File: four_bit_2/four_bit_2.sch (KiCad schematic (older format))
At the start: 1 part, among them P1 DIN_41612_128P

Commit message: Added in WHOMP, whatever it is
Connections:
- net CI09/: now also P1.60 (28B); no longer P1.59 (27B)
- net CO10: now also P1.61 (29B); no longer P1.60 (28B)
- net G05/: now also P1.62 (30B); no longer P1.61 (29B)
- net G06/: now also P1.63 (31B); no longer P1.62 (30B)
- net G07/: now also P1.64 (32B); no longer P1.63 (31B)
- net GND: no longer P1.71 (7C)
- net L08/: now also P1.65 (1C); no longer P1.64 (32B)
- net WL05/: now also P1.68 (4C); no longer P1.67 (3C)
- net WL06/: now also P1.69 (5C); no longer P1.68 (4C)
- net WL07/: now also P1.70 (6C); no longer P1.69 (5C)
- net WL08/: now also P1.71 (7C); no longer P1.70 (6C)
- net XUY05/: now also P1.66 (2C); no longer P1.65 (1C)
- net XUY06/: now also P1.67 (3C); no longer P1.66 (2C)
- new net WHOMP: P1.59 (27B)
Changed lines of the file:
@@
 $EndDescr
 $Sheet
-S 1750 1200 1400 7250
+S 1750 1200 1400 7600
 U 5692835C
 F0 "A09_1" 60
@@
 F60 "_WL1" O R 3150 4050 60
 F61 "_WL1/" O R 3150 4150 60
-F62 "_MWL1" O R 3150 4600 60
+F62 "_MWL1" O R 3150 4750 60
 F63 "_CI_OUT" O R 3150 2750 60
 F64 "_CO_IN" I L 1750 3650 60
@@
 F96 "_WL2" O R 3150 4250 60
 F97 "_WL2/" O R 3150 4350 60
-F98 "_MWL2" O R 3150 4700 60
+F98 "_MWL2" O R 3150 4850 60
 F99 "_RL1/" O R 3150 3850 60
 F100 "_RL2/" O R 3150 3950 60
+F101 "_RL_OUT_2" O R 3150 4600 60
+F102 "_RL_OUT_1" O R 3150 4500 60
+F103 "_WHOMPA" I L 1750 8700 60
+F104 "_WHOMP_1" I L 1750 8500 60
+F105 "_WHOMP_2" I L 1750 8600 60
 $EndSheet
 $Comp
@@
 $EndComp
 $Sheet
-S 4400 1200 1400 7250
+S 4400 1200 1400 7600
 U 56928367
 F0 "A09_2" 60
@@
 F60 "_WL1" O R 5800 4050 60
 F61 "_WL1/" O R 5800 4150 60
-F62 "_MWL1" O R 5800 4600 60
+F62 "_MWL1" O R 5800 4700 60
 F63 "_CI_OUT" O R 5800 2750 60
 F64 "_CO_IN" I L 4400 3650 60
@@
 F96 "_WL2" O R 5800 4250 60
 F97 "_WL2/" O R 5800 4350 60
-F98 "_MWL2" O R 5800 4700 60
+F98 "_MWL2" O R 5800 4850 60
 F99 "_RL1/" O R 5800 3850 60
 F100 "_RL2/" O R 5800 3950 60
+F101 "_RL_OUT_2" O R 5800 4600 60
+F102 "_RL_OUT_1" O R 5800 4500 60
+F103 "_WHOMPA" I L 4400 8700 60
+F104 "_WHOMP_1" I L 4400 8500 60
+F105 "_WHOMP_2" I L 4400 8600 60
 $EndSheet
 Text GLabel 1650 1300 0    60   Input ~ 0
@@
 	4400 8350 4300 8350
 Wire Wire Line
-	9700 1550 9800 1550
-Wire Wire Line
 	9700 1650 9800 1650
-Connection ~ 9700 1650
 Wire Wire Line
 	9700 1750 9800 1750
@@
 Wire Wire Line
 	5800 1800 5900 1800
-Text GLabel 8750 3750 0    60   Input ~ 0
+Text GLabel 8750 3850 0    60   Input ~ 0
 G05/
-Text GLabel 8750 3850 0    60   Input ~ 0
+Text GLabel 8750 3950 0    60   Input ~ 0
 G06/
-Text GLabel 8750 3950 0    60   Input ~ 0
+Text GLabel 8750 4050 0    60   Input ~ 0
 G07/
 Wire Wire Line
-	8850 3750 8750 3750
-Wire Wire Line
 	8850 3850 8750 3850
 Wire Wire Line
 	8850 3950 8750 3950
 Wire Wire Line
-	9700 1550 9700 4200
+	8850 4050 8750 4050
+Wire Wire Line
+	9700 1650 9700 4200
 Text GLabel 3250 3350 2    60   Output ~ 0
 XUY05/
@@
 Wire Wire Line
 	3150 3450 3250 3450
-Text GLabel 9700 950  0    60   Input ~ 0
+Text GLabel 9700 1050 0    60   Input ~ 0
 XUY05/
-Text GLabel 9700 1050 0    60   Input ~ 0
+Text GLabel 9700 1150 0    60   Input ~ 0
 XUY06/
 Wire Wire Line
-	8850 4050 8750 4050
-Wire Wire Line
-	9800 1050 9700 1050
-Text GLabel 9700 1150 0    60   Input ~ 0
-WL05/
+	9800 950  9700 950
 Wire Wire Line
 	9800 1150 9700 1150
 Text GLabel 9700 1250 0    60   Input ~ 0
-WL06/
+WL05/
 Wire Wire Line
 	9800 1250 9700 1250
 Text GLabel 9700 1350 0    60   Input ~ 0
-WL07/
+WL06/
 Wire Wire Line
 	9800 1350 9700 1350
 Text GLabel 9700 1450 0    60   Input ~ 0
+WL07/
+Wire Wire Line
+	9800 1450 9700 1450
+Text GLabel 9700 1550 0    60   Input ~ 0
 WL08/
 Wire Wire Line
-	9800 1450 9700 1450
+	9800 1550 9700 1550
 Text GLabel 5900 2750 2    60   Output ~ 0
 CI09/
@@
 Wire Wire Line
 	5800 2850 5900 2850
-Text GLabel 8750 3550 0    60   Input ~ 0
+Text GLabel 8750 3650 0    60   Input ~ 0
 CI09/
-Text GLabel 8750 3650 0    60   Input ~ 0
+Text GLabel 8750 3750 0    60   Input ~ 0
 CO10
 Wire Wire Line
-	8850 3550 8750 3550
-Wire Wire Line
 	8850 3650 8750 3650
+Wire Wire Line
+	8850 3750 8750 3750
 Text Label 3250 2200 0    60   ~ 0
 L06/
@@
 	5800 2200 5900 2200
 Wire Wire Line
-	9700 950  9800 950
-Text GLabel 8750 4050 0    60   Input ~ 0
+	9700 1050 9800 1050
+Text GLabel 9700 950  0    60   Input ~ 0
 L08/
+Wire Wire Line
+	1750 8600 1200 8600
+Wire Wire Line
+	1200 8500 1200 8750
+Wire Wire Line
+	1750 8700 1200 8700
+Connection ~ 1200 8700
+$Comp
+L GND #PWR011
+U 1 1 56C64D2D
+P 1200 8750
+F 0 "#PWR011" H 1200 8500 50  0001 C CNN
+F 1 "GND" H 1200 8600 50  0000 C CNN
+F 2 "" H 1200 8750 60  0000 C CNN
+F 3 "" H 1200 8750 60  0000 C CNN
+	1    1200 8750
+	1    0    0    -1
+$EndComp
+Wire Wire Line
+	1200 8500 1750 8500
+Connection ~ 1200 8600
+Wire Wire Line
+	4400 8600 3850 8600
+Wire Wire Line
+	3850 8600 3850 8750
+Wire Wire Line
+	4400 8700 3850 8700
+Connection ~ 3850 8700
+$Comp
+L GND #PWR012
+U 1 1 56C696A6
+P 3850 8750
+F 0 "#PWR012" H 3850 8500 50  0001 C CNN
+F 1 "GND" H 3850 8600 50  0000 C CNN
+F 2 "" H 3850 8750 60  0000 C CNN
+F 3 "" H 3850 8750 60  0000 C CNN
+	1    3850 8750
+	1    0    0    -1
+$EndComp
+Text GLabel 4300 8500 0    60   Input ~ 0
+WHOMP
+Wire Wire Line
+	4400 8500 4300 8500
+Text GLabel 8750 3550 0    60   Output ~ 0
+WHOMP
+Wire Wire Line
+	8850 3550 8750 3550
 $EndSCHEMATC

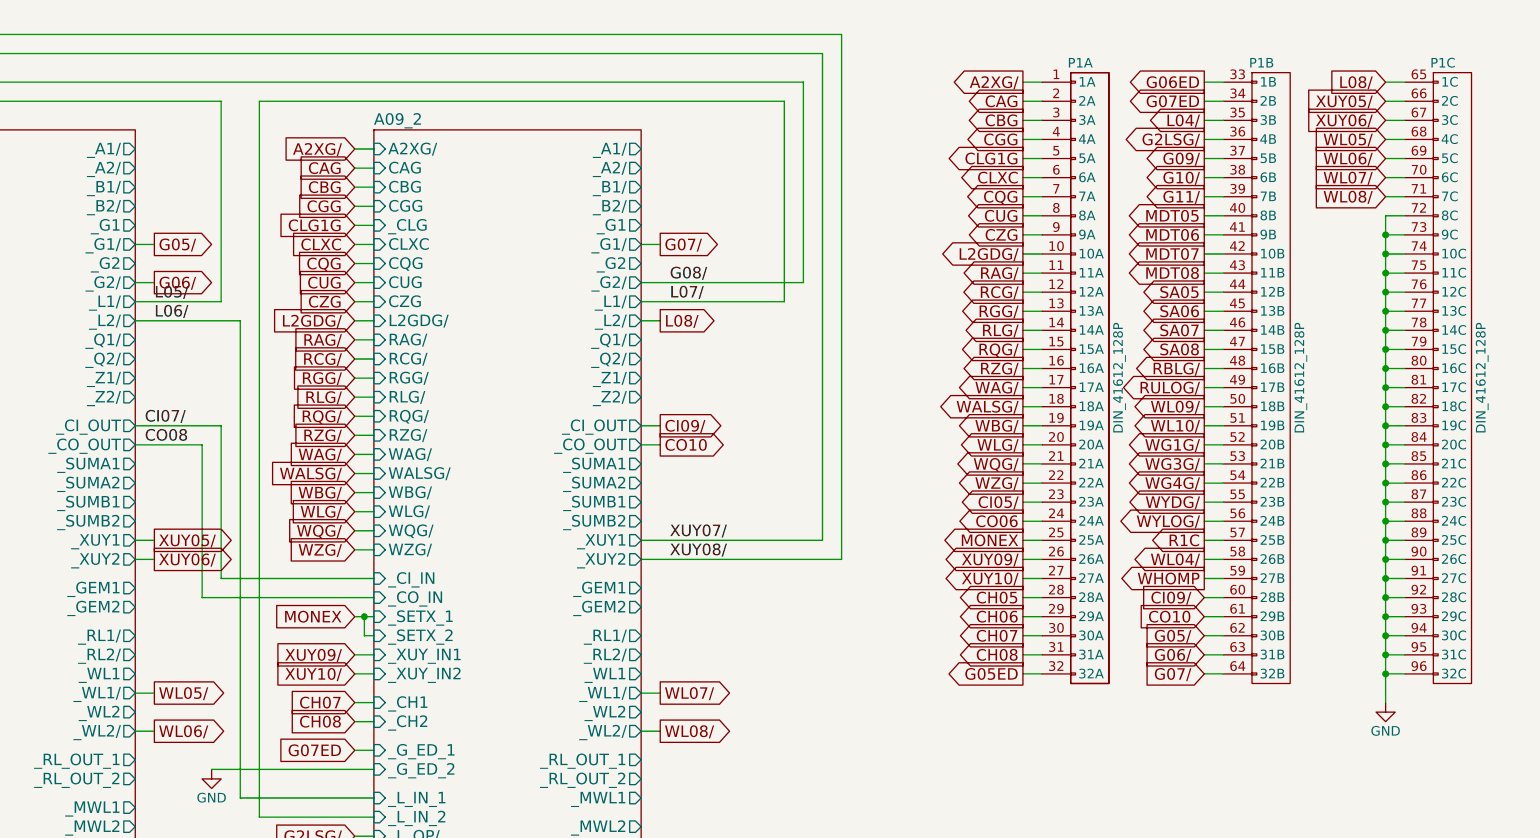
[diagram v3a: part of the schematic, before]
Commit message: Added and tied in module 12, parity & s register
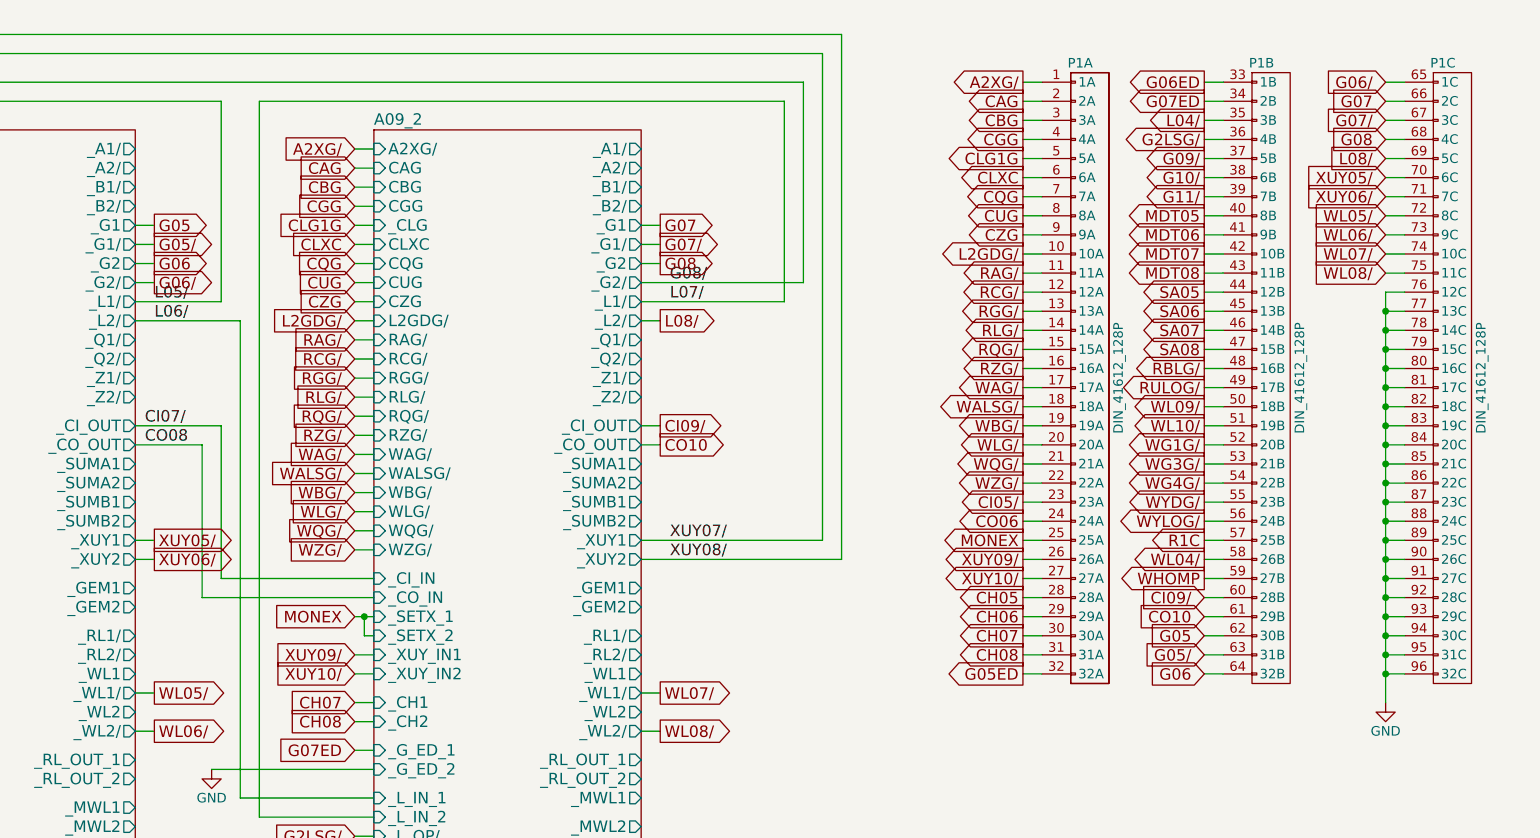
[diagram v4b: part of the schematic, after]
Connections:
- net G05/: now also P1.63 (31B); no longer P1.62 (30B)
- net G06/: now also P1.65 (1C); no longer P1.63 (31B)
- net G07/: now also P1.67 (3C); no longer P1.64 (32B)
- net GND: no longer P1.72 (8C), P1.73 (9C), P1.74 (10C), P1.75 (11C)
- net L08/: now also P1.69 (5C); no longer P1.65 (1C)
- net WL05/: now also P1.72 (8C); no longer P1.68 (4C)
- net WL06/: now also P1.73 (9C); no longer P1.69 (5C)
- net WL07/: now also P1.74 (10C); no longer P1.70 (6C)
- net WL08/: now also P1.75 (11C); no longer P1.71 (7C)
- net XUY05/: now also P1.70 (6C); no longer P1.66 (2C)
- net XUY06/: now also P1.71 (7C); no longer P1.67 (3C)
- new net G05: P1.62 (30B)
- new net G06: P1.64 (32B)
- new net G07: P1.66 (2C)
- new net G08: P1.68 (4C)
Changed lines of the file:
@@
 	4400 8350 4300 8350
 Wire Wire Line
-	9700 1650 9800 1650
-Wire Wire Line
-	9700 1750 9800 1750
-Connection ~ 9700 1750
-Wire Wire Line
-	9700 1850 9800 1850
-Connection ~ 9700 1850
-Wire Wire Line
-	9700 1950 9800 1950
-Connection ~ 9700 1950
-Wire Wire Line
 	9700 2050 9800 2050
-Connection ~ 9700 2050
 Wire Wire Line
 	9700 2150 9800 2150
@@
 Wire Wire Line
 	5800 1800 5900 1800
-Text GLabel 8750 3850 0    60   Input ~ 0
+Text GLabel 8750 3950 0    60   Input ~ 0
 G05/
-Text GLabel 8750 3950 0    60   Input ~ 0
+Text GLabel 9700 950  0    60   Input ~ 0
 G06/
-Text GLabel 8750 4050 0    60   Input ~ 0
+Text GLabel 9700 1150 0    60   Input ~ 0
 G07/
 Wire Wire Line
-	8850 3850 8750 3850
-Wire Wire Line
 	8850 3950 8750 3950
 Wire Wire Line
-	8850 4050 8750 4050
-Wire Wire Line
-	9700 1650 9700 4200
+	9800 950  9700 950
+Wire Wire Line
+	9800 1150 9700 1150
 Text GLabel 3250 3350 2    60   Output ~ 0
 XUY05/
@@
 Wire Wire Line
 	3150 3450 3250 3450
-Text GLabel 9700 1050 0    60   Input ~ 0
+Text GLabel 9700 1450 0    60   Input ~ 0
 XUY05/
-Text GLabel 9700 1150 0    60   Input ~ 0
+Text GLabel 9700 1550 0    60   Input ~ 0
 XUY06/
 Wire Wire Line
-	9800 950  9700 950
-Wire Wire Line
-	9800 1150 9700 1150
-Text GLabel 9700 1250 0    60   Input ~ 0
+	9800 1350 9700 1350
+Wire Wire Line
+	9800 1550 9700 1550
+Text GLabel 9700 1650 0    60   Input ~ 0
 WL05/
 Wire Wire Line
-	9800 1250 9700 1250
-Text GLabel 9700 1350 0    60   Input ~ 0
+	9800 1650 9700 1650
+Text GLabel 9700 1750 0    60   Input ~ 0
 WL06/
 Wire Wire Line
-	9800 1350 9700 1350
-Text GLabel 9700 1450 0    60   Input ~ 0
+	9800 1750 9700 1750
+Text GLabel 9700 1850 0    60   Input ~ 0
 WL07/
 Wire Wire Line
-	9800 1450 9700 1450
-Text GLabel 9700 1550 0    60   Input ~ 0
+	9800 1850 9700 1850
+Text GLabel 9700 1950 0    60   Input ~ 0
 WL08/
 Wire Wire Line
-	9800 1550 9700 1550
+	9800 1950 9700 1950
 Text GLabel 5900 2750 2    60   Output ~ 0
 CI09/
@@
 	5800 2200 5900 2200
 Wire Wire Line
-	9700 1050 9800 1050
-Text GLabel 9700 950  0    60   Input ~ 0
+	9700 1450 9800 1450
+Text GLabel 9700 1350 0    60   Input ~ 0
 L08/
 Wire Wire Line
@@
 Wire Wire Line
 	8850 3550 8750 3550
+Text GLabel 3250 1700 2    60   Output ~ 0
+G05
+Wire Wire Line
+	3150 1700 3250 1700
+Text GLabel 3250 1900 2    60   Output ~ 0
+G06
+Wire Wire Line
+	3150 1900 3250 1900
+Text GLabel 5900 1700 2    60   Output ~ 0
+G07
+Wire Wire Line
+	5800 1700 5900 1700
+Text GLabel 5900 1900 2    60   Output ~ 0
+G08
+Wire Wire Line
+	5800 1900 5900 1900
+Wire Wire Line
+	9700 2050 9700 4200
+Text GLabel 8750 3850 0    60   Input ~ 0
+G05
+Wire Wire Line
+	8850 3850 8750 3850
+Text GLabel 8750 4050 0    60   Input ~ 0
+G06
+Wire Wire Line
+	8850 4050 8750 4050
+Text GLabel 9700 1050 0    60   Input ~ 0
+G07
+Wire Wire Line
+	9800 1050 9700 1050
+Text GLabel 9700 1250 0    60   Input ~ 0
+G08
+Wire Wire Line
+	9800 1250 9700 1250
 $EndSCHEMATC

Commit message: Added and tied in module 15, the rupt service (and banking/rope+strand selection)
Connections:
- net GND: no longer P1.76 (12C), P1.77 (13C)
- net WL05/: now also P1.74 (10C); no longer P1.72 (8C)
- net WL06/: now also P1.75 (11C); no longer P1.73 (9C)
- net WL07/: now also P1.76 (12C); no longer P1.74 (10C)
- net WL08/: now also P1.77 (13C); no longer P1.75 (11C)
- net XUY05/: now also P1.72 (8C); no longer P1.70 (6C)
- net XUY06/: now also P1.73 (9C); no longer P1.71 (7C)
- new net RL05/: P1.70 (6C)
- new net RL06/: P1.71 (7C)
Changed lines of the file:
@@
 	4400 8350 4300 8350
 Wire Wire Line
-	9700 2050 9800 2050
-Wire Wire Line
-	9700 2150 9800 2150
-Connection ~ 9700 2150
-Wire Wire Line
-	9700 2250 9800 2250
-Connection ~ 9700 2250
-Wire Wire Line
-	9700 2350 9800 2350
-Connection ~ 9700 2350
-Wire Wire Line
 	9700 2450 9800 2450
-Connection ~ 9700 2450
 Wire Wire Line
 	9700 2550 9800 2550
@@
 Wire Wire Line
 	3150 3450 3250 3450
-Text GLabel 9700 1450 0    60   Input ~ 0
+Text GLabel 9700 1650 0    60   Input ~ 0
 XUY05/
-Text GLabel 9700 1550 0    60   Input ~ 0
+Text GLabel 9700 1750 0    60   Input ~ 0
 XUY06/
 Wire Wire Line
 	9800 1350 9700 1350
-Wire Wire Line
-	9800 1550 9700 1550
-Text GLabel 9700 1650 0    60   Input ~ 0
-WL05/
-Wire Wire Line
-	9800 1650 9700 1650
-Text GLabel 9700 1750 0    60   Input ~ 0
-WL06/
 Wire Wire Line
 	9800 1750 9700 1750
 Text GLabel 9700 1850 0    60   Input ~ 0
-WL07/
+WL05/
 Wire Wire Line
 	9800 1850 9700 1850
 Text GLabel 9700 1950 0    60   Input ~ 0
+WL06/
+Wire Wire Line
+	9800 1950 9700 1950
+Text GLabel 9700 2050 0    60   Input ~ 0
+WL07/
+Wire Wire Line
+	9800 2050 9700 2050
+Text GLabel 9700 2150 0    60   Input ~ 0
 WL08/
 Wire Wire Line
-	9800 1950 9700 1950
+	9800 2150 9700 2150
 Text GLabel 5900 2750 2    60   Output ~ 0
 CI09/
@@
 	5800 2200 5900 2200
 Wire Wire Line
-	9700 1450 9800 1450
+	9700 1650 9800 1650
 Text GLabel 9700 1350 0    60   Input ~ 0
 L08/
@@
 Wire Wire Line
 	5800 1900 5900 1900
-Wire Wire Line
-	9700 2050 9700 4200
 Text GLabel 8750 3850 0    60   Input ~ 0
 G05
@@
 Wire Wire Line
 	9800 1250 9700 1250
+Text GLabel 3250 3850 2    60   BiDi ~ 0
+RL05/
+Wire Wire Line
+	3150 3850 3250 3850
+Text GLabel 3250 3950 2    60   BiDi ~ 0
+RL06/
+Wire Wire Line
+	3150 3950 3250 3950
+Text GLabel 9700 1450 0    60   BiDi ~ 0
+RL05/
+Wire Wire Line
+	9800 1450 9700 1450
+Text GLabel 9700 1550 0    60   BiDi ~ 0
+RL06/
+Wire Wire Line
+	9800 1550 9700 1550
+Wire Wire Line
+	9700 2250 9700 4200
+Wire Wire Line
+	9700 2350 9800 2350
+Connection ~ 9700 2450
+Wire Wire Line
+	9700 2250 9800 2250
+Connection ~ 9700 2350
 $EndSCHEMATC

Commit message: Added erasable memory, and fixed lots of random wiring errors.
I decided to go with a 16-bit-wide MRAM chip -- I had  no idea
until I started researching RAM options how technologically
similar MRAM is to core memory. The datasheet diagrams look like
they're straight out of the AGC documentation!

There's a slight inaccuracy in this implementation worth mentioning.
Like fixed memory, I've wired the sense amplifier outputs directly up
to the tristate data output pins of the MRAM chip. But because the
data lines are bidirectional, data being written into RAM will show up
on the sense lines, and go straight into the ungated G register. Since
G is what's being written out, this doesn't matter 99% of the time, but
if there's an overflow condition in G (I don't even know if this is
possible), the bit 16 will be copied over bit 16, and the overflow
condition will be lost. I'll keep an eye out to see if anything relies
on G not changing after the write cycle is complete.

With erasable memory introduced, the computer now theoretically supports
all programs that don't use I/O or interrupts. I've started running
the VirtualAGC validation program, and have been fixing random errors
uncovered by failing self-tests.
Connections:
- net GND: no longer P1.78 (14C), P1.79 (15C), P1.80 (16C), P1.81 (17C)
- new net GEM05: P1.78 (14C)
- new net GEM06: P1.79 (15C)
- new net GEM07: P1.80 (16C)
- new net GEM08: P1.81 (17C)
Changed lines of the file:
@@
 	4400 8350 4300 8350
 Wire Wire Line
-	9700 2450 9800 2450
-Wire Wire Line
-	9700 2550 9800 2550
-Connection ~ 9700 2550
-Wire Wire Line
 	9700 2650 9800 2650
-Connection ~ 9700 2650
 Wire Wire Line
 	9700 2750 9800 2750
@@
 Wire Wire Line
 	9800 1550 9700 1550
-Wire Wire Line
-	9700 2250 9700 4200
-Wire Wire Line
-	9700 2350 9800 2350
-Connection ~ 9700 2450
-Wire Wire Line
-	9700 2250 9800 2250
-Connection ~ 9700 2350
+Text GLabel 3250 3600 2    60   Output ~ 0
+GEM05
+Wire Wire Line
+	3150 3600 3250 3600
+Text GLabel 3250 3700 2    60   Output ~ 0
+GEM06
+Wire Wire Line
+	3150 3700 3250 3700
+Text GLabel 5900 3600 2    60   Output ~ 0
+GEM07
+Wire Wire Line
+	5800 3600 5900 3600
+Text GLabel 5900 3700 2    60   Output ~ 0
+GEM08
+Wire Wire Line
+	5800 3700 5900 3700
+Wire Wire Line
+	9700 2650 9700 4200
+Text GLabel 9700 2250 0    60   Input ~ 0
+GEM05
+Wire Wire Line
+	9800 2250 9700 2250
+Text GLabel 9700 2350 0    60   Input ~ 0
+GEM06
+Wire Wire Line
+	9800 2350 9700 2350
+Text GLabel 9700 2450 0    60   Input ~ 0
+GEM07
+Wire Wire Line
+	9800 2450 9700 2450
+Text GLabel 9700 2550 0    60   Input ~ 0
+GEM08
+Wire Wire Line
+	9800 2550 9700 2550
 $EndSCHEMATC

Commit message: Added and tied in Inout VII, the final logic module!
I still need to comb through the schematics to see if there are any
stray gates I missed. The initial conditions are also pretty much
guaranteed to be wrong. But it's mostly all there!
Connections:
- net GEM05: now also P1.82 (18C); no longer P1.78 (14C)
- net GEM06: now also P1.83 (19C); no longer P1.79 (15C)
- net GEM07: now also P1.84 (20C); no longer P1.80 (16C)
- net GEM08: now also P1.85 (21C); no longer P1.81 (17C)
- net GND: no longer P1.82 (18C), P1.83 (19C), P1.84 (20C), P1.85 (21C)
- net WL05/: now also P1.75 (11C); no longer P1.74 (10C)
- net WL06/: now also P1.77 (13C); no longer P1.75 (11C)
- net WL07/: now also P1.79 (15C); no longer P1.76 (12C)
- net WL08/: now also P1.81 (17C); no longer P1.77 (13C)
- new net WL05: P1.74 (10C)
- new net WL06: P1.76 (12C)
- new net WL07: P1.78 (14C)
- new net WL08: P1.80 (16C)
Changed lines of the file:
@@
 	4400 8350 4300 8350
 Wire Wire Line
-	9700 2650 9800 2650
-Wire Wire Line
-	9700 2750 9800 2750
-Connection ~ 9700 2750
-Wire Wire Line
-	9700 2850 9800 2850
-Connection ~ 9700 2850
-Wire Wire Line
-	9700 2950 9800 2950
-Connection ~ 9700 2950
-Wire Wire Line
 	9700 3050 9800 3050
-Connection ~ 9700 3050
 Wire Wire Line
 	9700 3150 9800 3150
@@
 Wire Wire Line
 	9800 1750 9700 1750
-Text GLabel 9700 1850 0    60   Input ~ 0
+Text GLabel 9700 1950 0    60   Input ~ 0
 WL05/
 Wire Wire Line
-	9800 1850 9700 1850
-Text GLabel 9700 1950 0    60   Input ~ 0
+	9800 1950 9700 1950
+Text GLabel 9700 2150 0    60   Input ~ 0
 WL06/
 Wire Wire Line
-	9800 1950 9700 1950
-Text GLabel 9700 2050 0    60   Input ~ 0
+	9800 2150 9700 2150
+Text GLabel 9700 2350 0    60   Input ~ 0
 WL07/
 Wire Wire Line
-	9800 2050 9700 2050
-Text GLabel 9700 2150 0    60   Input ~ 0
+	9800 2350 9700 2350
+Text GLabel 9700 2550 0    60   Input ~ 0
 WL08/
 Wire Wire Line
-	9800 2150 9700 2150
+	9800 2550 9700 2550
 Text GLabel 5900 2750 2    60   Output ~ 0
 CI09/
@@
 Wire Wire Line
 	5800 3700 5900 3700
-Wire Wire Line
-	9700 2650 9700 4200
+Text GLabel 9700 2650 0    60   Input ~ 0
+GEM05
+Wire Wire Line
+	9800 2650 9700 2650
+Text GLabel 9700 2750 0    60   Input ~ 0
+GEM06
+Wire Wire Line
+	9800 2750 9700 2750
+Text GLabel 9700 2850 0    60   Input ~ 0
+GEM07
+Wire Wire Line
+	9800 2850 9700 2850
+Text GLabel 9700 2950 0    60   Input ~ 0
+GEM08
+Wire Wire Line
+	9800 2950 9700 2950
+Text GLabel 3250 4050 2    60   Output ~ 0
+WL05
+Text GLabel 3250 4250 2    60   Output ~ 0
+WL06
+Wire Wire Line
+	3150 4050 3250 4050
+Wire Wire Line
+	3150 4250 3250 4250
+Text GLabel 5900 4050 2    60   Output ~ 0
+WL07
+Text GLabel 5900 4250 2    60   Output ~ 0
+WL08
+Wire Wire Line
+	5800 4050 5900 4050
+Wire Wire Line
+	5800 4250 5900 4250
+Wire Wire Line
+	9700 3050 9700 4200
+Text GLabel 9700 2450 0    60   Input ~ 0
+WL08
+Wire Wire Line
+	9800 2450 9700 2450
 Text GLabel 9700 2250 0    60   Input ~ 0
-GEM05
+WL07
 Wire Wire Line
 	9800 2250 9700 2250
-Text GLabel 9700 2350 0    60   Input ~ 0
-GEM06
-Wire Wire Line
-	9800 2350 9700 2350
-Text GLabel 9700 2450 0    60   Input ~ 0
-GEM07
-Wire Wire Line
-	9800 2450 9700 2450
-Text GLabel 9700 2550 0    60   Input ~ 0
-GEM08
-Wire Wire Line
-	9800 2550 9700 2550
+Text GLabel 9700 2050 0    60   Input ~ 0
+WL06
+Wire Wire Line
+	9800 2050 9700 2050
+Text GLabel 9700 1850 0    60   Input ~ 0
+WL05
+Wire Wire Line
+	9800 1850 9700 1850
 $EndSCHEMATC
